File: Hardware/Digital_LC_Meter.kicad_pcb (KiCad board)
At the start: 2 copper layers, 160 x 99.1 mm, 29 parts

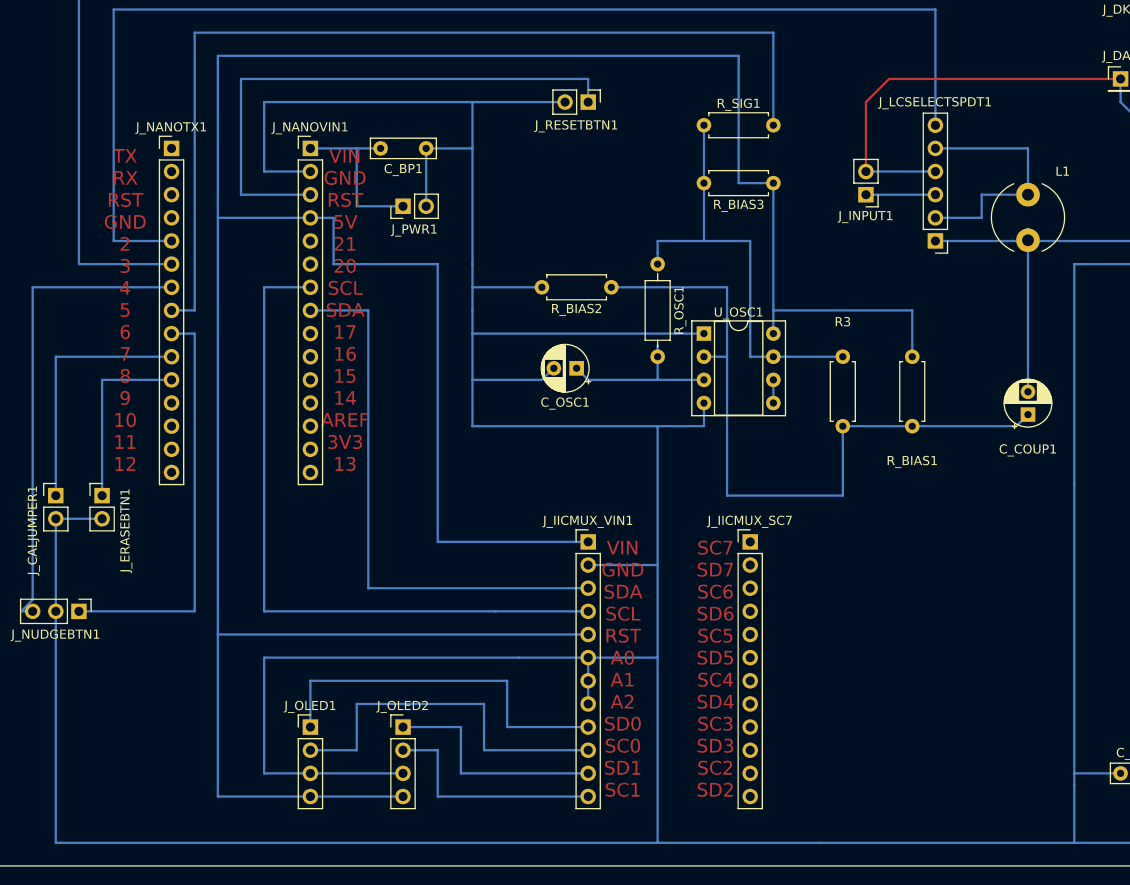
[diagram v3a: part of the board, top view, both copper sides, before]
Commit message: fixed OLED screen wiring on prototype, updated schematic and layout
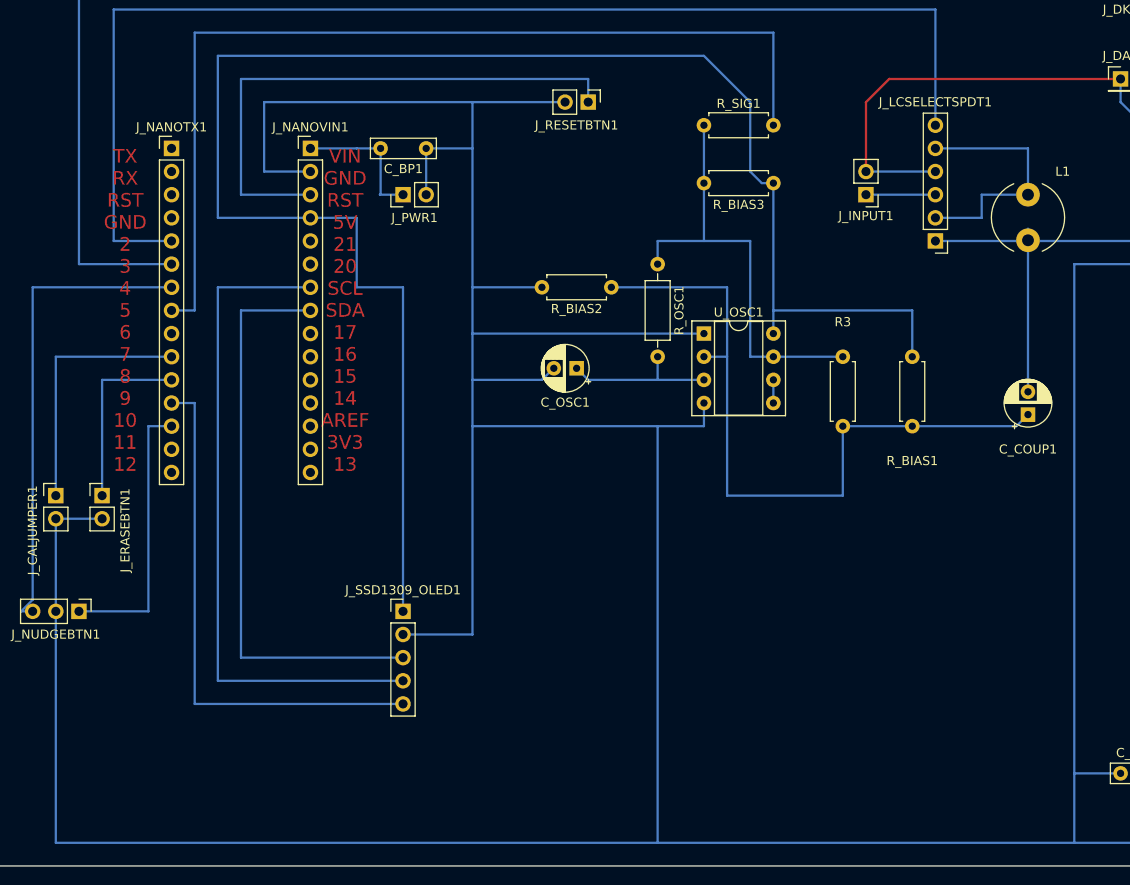
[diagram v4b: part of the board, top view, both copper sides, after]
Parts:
- removed J_IICMUX_SC7, J_IICMUX_VIN1: Conn_01x12, Connector_PinHeader_2.54mm:PinHeader_1x12_P2.54mm_Vertical
- removed J_OLED1, J_OLED2: Conn_01x04, Connector_PinHeader_2.54mm:PinHeader_1x04_P2.54mm_Vertical
- added J_SSD1309_OLED1: Conn_01x05, Connector_PinHeader_2.54mm:PinHeader_1x05_P2.54mm_Vertical, F.Cu at (78.7, 144.8)
- moved J_PWR1 1.27 mm to (78.7, 99.1)
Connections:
- J_NANOTX1 pad 1: Net-(J_NANOTX1-Pad1) -> (no net)
- J_NANOTX1 pad 12: Net-(J_NANOTX1-Pad12) -> /SRST
- J_NANOTX1 pad 13: Net-(J_NANOTX1-Pad13) -> /INCR_PIN10
- J_NANOTX1 pad 14: Net-(J_NANOTX1-Pad14) -> (no net)
- J_NANOTX1 pad 15: Net-(J_NANOTX1-Pad15) -> (no net)
- J_NANOTX1 pad 2: Net-(J_NANOTX1-Pad2) -> (no net)
- J_NANOTX1 pad 3: Net-(J_NANOTX1-Pad3) -> (no net)
- J_NANOTX1 pad 4: Net-(J_NANOTX1-Pad4) -> (no net)
- J_NANOTX1 pad 9: /INCR_PIN6 -> (no net)
- J_NANOVIN1 pad 10: Net-(J_NANOVIN1-Pad10) -> (no net)
- J_NANOVIN1 pad 11: Net-(J_NANOVIN1-Pad11) -> (no net)
- J_NANOVIN1 pad 12: Net-(J_NANOVIN1-Pad12) -> (no net)
- J_NANOVIN1 pad 13: Net-(J_NANOVIN1-Pad13) -> (no net)
- J_NANOVIN1 pad 14: Net-(J_NANOVIN1-Pad14) -> (no net)
- J_NANOVIN1 pad 15: Net-(J_NANOVIN1-Pad15) -> (no net)
- J_NANOVIN1 pad 5: Net-(J_NANOVIN1-Pad5) -> (no net)
- J_NANOVIN1 pad 6: Net-(J_NANOVIN1-Pad6) -> (no net)
- J_NANOVIN1 pad 9: Net-(J_NANOVIN1-Pad9) -> (no net)
- J_NUDGEBTN1 pad 1: /INCR_PIN6 -> /INCR_PIN10
- U_RLY1 pad 14: Net-(U_RLY1-Pad14) -> (no net)
- U_RLY1 pad 2: Net-(U_RLY1-Pad2) -> (no net)
- U_RLY1 pad 7: Net-(U_RLY1-Pad7) -> (no net)
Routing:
- net /5V: track 330.2 -> 189.3 mm
- net /SRST: track 0.00 -> 58.4 mm
- net /GND: track 678.3 -> 623.7 mm
- net /INCR_PIN6: track 45.7 -> 0.00 mm
- net /SCL0: track 40.6 -> 0.00 mm
- net /SDA0: track 40.6 -> 0.00 mm
- net /INCR_PIN10: track 0.00 -> 31.2 mm
- net /SDA1: track 25.4 -> 0.00 mm
- net /SCL1: track 25.4 -> 0.00 mm
- net /VIN: track 19.0 -> 15.3 mm
- net /SCL: track 76.2 -> 73.7 mm
- net /SDA: track 61.0 -> 63.5 mm
- net Net-(C_OSC1-Pad1): track 18.3 -> 17.0 mm
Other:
- board text added: "5V GND SDA SCL RST"
- board text removed: "SC7 SD7 SC6 SD6 SC5 SD5 SC4 SD4 SC3 SD3 SC2 SD2"
- board text removed: "VIN GND SDA SCL RST A0 A1 A2 SD0 SC0 SD1 SC1"

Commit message: updated docs
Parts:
- moved C_COUP1 47.8 mm to (184.2, 92.7)
- moved J_CALJUMPER1 47.8 mm to (77.5, 101.6)
- moved J_DK1 47.8 mm to (194.3, 45.7)
- moved J_ERASEBTN1 47.8 mm to (82.5, 101.6)
- moved J_INPUT1 47.8 mm to (166.4, 68.6)
- moved J_LCSELECTSPDT1 47.8 mm to (174.0, 73.7)
- moved L1 47.8 mm to (184.2, 68.6)
- moved R3 47.8 mm to (163.8, 86.4)
- moved R_BIAS2 47.8 mm to (138.4, 78.7)
- moved R_BIAS3 47.8 mm to (156.2, 67.3)
- moved C_BP1 47.8 mm to (118.1, 63.5)
- moved C_MICA1 47.8 mm to (194.3, 132.1)
- moved C_MICA2 47.8 mm to (204.5, 127.0)
- moved C_OSC1 47.8 mm to (134.6, 87.6)
- moved J_DA1 47.8 mm to (194.3, 55.9)
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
